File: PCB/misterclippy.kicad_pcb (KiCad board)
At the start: 2 copper layers, 75 parts, among them J1 PWR, J2 Output Gate, J3 Output Gate, J4 Input, J5 Input, J6 Through, J7 Through, J8 Audio In, J9 Audio In, Q1 BC547, Q2 BC547, U1 LM393, U2 TL072, U3 LM393, U4 TL072, U5 LM393

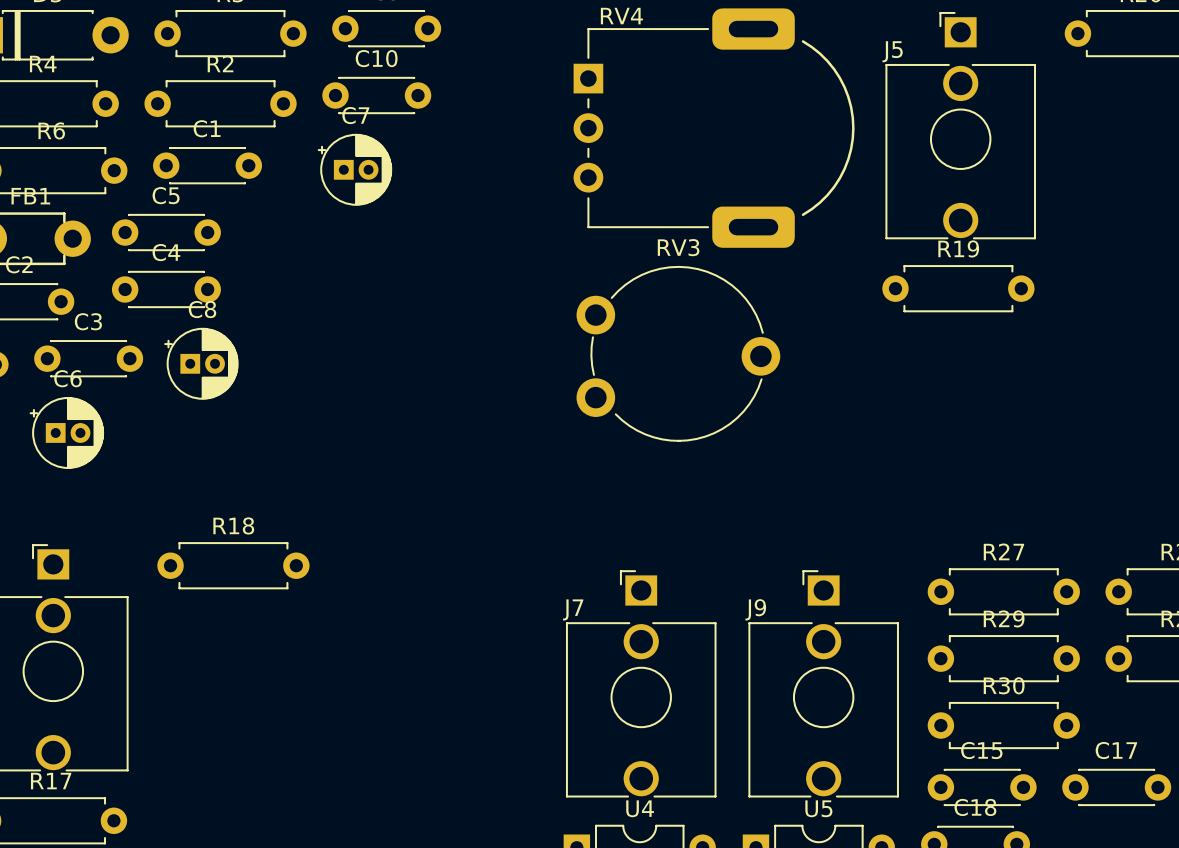
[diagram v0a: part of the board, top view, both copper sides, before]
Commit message: :wrench: Re-assign component designators
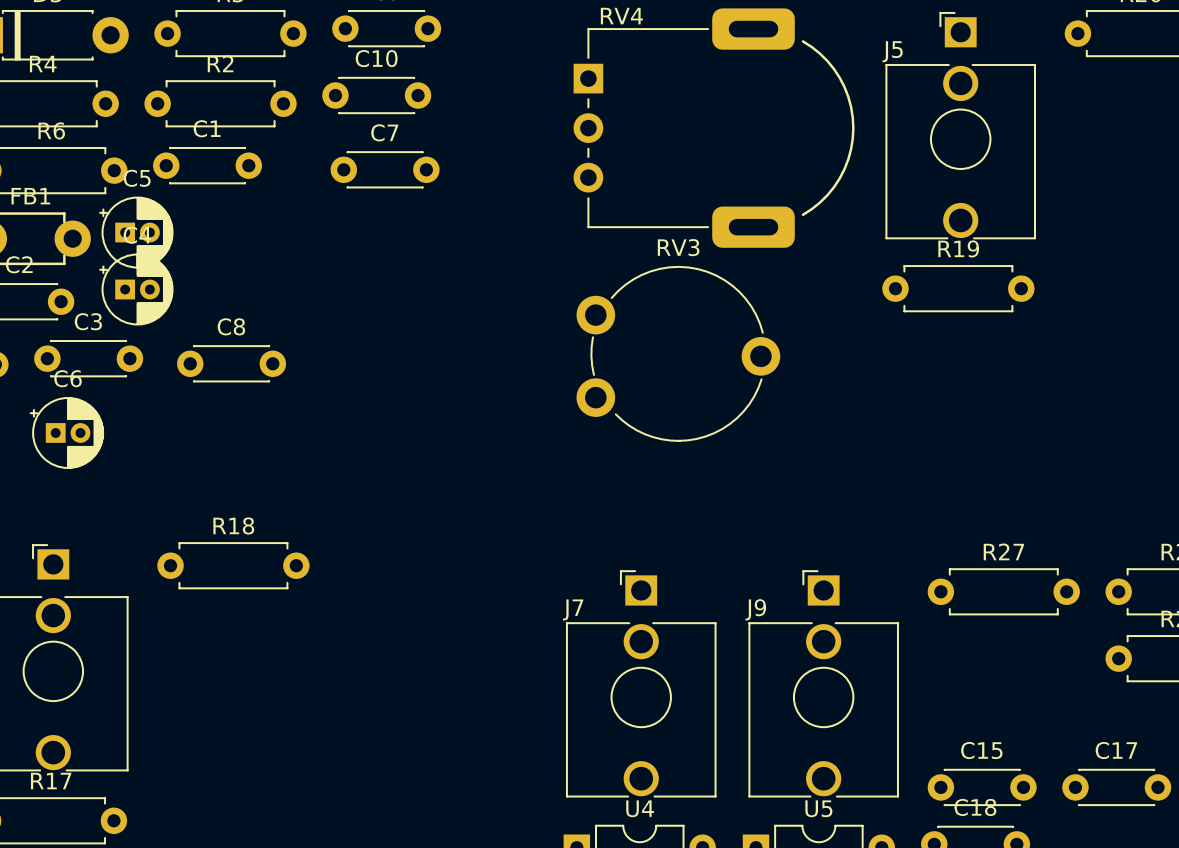
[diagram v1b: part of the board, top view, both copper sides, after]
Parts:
- removed R29, R30: 100k, Resistor_THT:R_Axial_DIN0207_L6.3mm_D2.5mm_P7.62mm_Horizontal
- C4, C5: value 100n -> 10u; footprint Capacitor_THT:C_Disc_D4.3mm_W1.9mm_P5.00mm -> Capacitor_THT:CP_Radial_D4.0mm_P1.50mm
- C7, C8: value 10u -> 100n; footprint Capacitor_THT:CP_Radial_D4.0mm_P1.50mm -> Capacitor_THT:C_Disc_D4.3mm_W1.9mm_P5.00mm
- J6: value Through -> Audio In
- J9: value Audio In -> Through
- R10, R15: value 2k2 -> 22k
- R11: value 10k -> 4k7
- R12, R7: value 22k -> 10k
- R13, R8: value 4k7 -> 2k2
- R16: value 10k -> 100k
- R19: value 22k -> 100k
- R22, R27: value 1k -> 100k
- R23, R28: value 100k -> 1k
- R5: value 47k -> 22k
- R6: value 100k -> 4k7
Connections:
- C1 pad 1: +12V -> +5V
- C10 pad 1: /Detector1/Clipped -> GND
- C2 pad 1: GND -> Net-(D2-K)
- C2 pad 2: -12V -> GND
- C3 pad 1: +5V -> GND
- C3 pad 2: GND -> Net-(D3-A)
- C4 pad 1: Net-(C4-Pad1) -> +5V
- C5 pad 1: GND -> +12V
- C5 pad 2: Net-(C5-Pad2) -> GND
- C6 pad 1: +5V -> GND
- C6 pad 2: GND -> -12V
- C7 pad 1: +12V -> /Detector 1/Clipped
- C7 pad 2: GND -> -12V
- C8 pad 1: GND -> /Detector 2/Clipped
- C9 pad 1: /Detector/Clipped -> +12V
- C9 pad 2: -12V -> GND
- D2 pad 1: Net-(C4-Pad1) -> Net-(D2-K)
- D3 pad 2: Net-(C5-Pad2) -> Net-(D3-A)
- D4 pad 1: Net-(D4-Pad1) -> Net-(D4-K)
- D5 pad 1: Net-(D5-Pad1) -> Net-(D5-K)
- FB1 pad 1: Net-(C4-Pad1) -> Net-(D2-K)
- FB2 pad 1: Net-(C5-Pad2) -> Net-(D3-A)
- J6 pad TN: unconnected-(J6-PadTN) -> GND
- J8 pad T: Net-(R21-Pad1) -> Net-(J8-PadT)
- J9 pad T: Net-(R26-Pad1) -> Net-(J9-PadT)
- J9 pad TN: GND -> unconnected-(J9-PadTN)
- Q1 pad 1: Net-(Q1-Pad1) -> Net-(Q1-C)
- Q1 pad 2: Net-(Q1-Pad2) -> Net-(Q1-B)
- Q2 pad 1: Net-(Q2-Pad1) -> Net-(Q2-C)
- Q2 pad 2: Net-(Q2-Pad2) -> Net-(Q2-B)
- R1 pad 2: /Detector/Clipped -> /Detector 1/Clipped
- R10 pad 1: +5V -> /Output 2/Clip Input
- R10 pad 2: Net-(Q1-Pad1) -> Net-(D5-K)
- R11 pad 1: Net-(Q1-Pad1) -> +5V
- R11 pad 2: Net-(J2-PadT) -> Net-(Q2-B)
- R12 pad 1: /output1/Clip Input -> Net-(Q2-B)
- R12 pad 2: Net-(D5-Pad1) -> /Output 2/Clip Input
- R13 pad 2: Net-(Q2-Pad2) -> Net-(Q2-C)
- R14 pad 1: Net-(Q2-Pad2) -> Net-(Q2-C)
- R14 pad 2: /output1/Clip Input -> Net-(J3-PadT)
- R15 pad 1: +5V -> +12V
- R15 pad 2: Net-(Q2-Pad1) -> Net-(R15-Pad2)
- R16 pad 1: Net-(Q2-Pad1) -> GND
- R16 pad 2: Net-(J3-PadT) -> Net-(R16-Pad2)
- R19 pad 1: +12V -> Net-(J6-PadT)
- R19 pad 2: Net-(R19-Pad2) -> Net-(U2A-+)
- R2 pad 2: /Detector1/Clipped -> /Detector 2/Clipped
- R20 pad 1: GND -> Net-(U3A--)
- R20 pad 2: Net-(R20-Pad2) -> /Clip CV 1/Clip CV
- R21 pad 1: Net-(R21-Pad1) -> Net-(U2B--)
- R21 pad 2: Net-(R21-Pad2) -> /Clip CV 1/Clip CV
- R22 pad 1: Audio Input -> Net-(U3B-+)
- R22 pad 2: Net-(J6-PadT) -> Net-(U2B--)
- R23 pad 1: Net-(R23-Pad1) -> Net-(J7-PadT)
- R23 pad 2: /Clip CV/Clip CV -> Net-(U2A--)
- R24 pad 1: Net-(R24-Pad1) -> Net-(J8-PadT)
- R24 pad 2: /Clip CV/Clip CV -> Net-(U4A-+)
- R25 pad 1: Net-(R25-Pad1) -> Net-(U5A--)
- R25 pad 2: Net-(R23-Pad1) -> /Clip CV 2/Clip CV
- R26 pad 1: Net-(R26-Pad1) -> Net-(U4B--)
- R26 pad 2: Net-(R26-Pad2) -> /Clip CV 2/Clip CV
- R27 pad 1: Audio Input -> Net-(U5B-+)
- R27 pad 2: Net-(J7-PadT) -> Net-(U4B--)
- R28 pad 1: Net-(R28-Pad1) -> Net-(J9-PadT)
- R28 pad 2: /Clip CV1/Clip CV -> Net-(U4A--)
- R3 pad 2: Net-(R3-Pad2) -> DELAY_THRESHOLD
- R4 pad 1: Net-(R3-Pad2) -> DELAY_THRESHOLD
- R5 pad 1: GND -> /Output 1/Clip Input
- R5 pad 2: Net-(R5-Pad2) -> Net-(D4-K)
- R6 pad 1: Net-(R5-Pad2) -> +5V
- R6 pad 2: -12V -> Net-(Q1-B)
- R7 pad 1: /output/Clip Input -> Net-(Q1-B)
- R7 pad 2: Net-(D4-Pad1) -> /Output 1/Clip Input
- R8 pad 2: Net-(Q1-Pad2) -> Net-(Q1-C)
- R9 pad 1: Net-(Q1-Pad2) -> Net-(Q1-C)
- R9 pad 2: /output/Clip Input -> Net-(J2-PadT)
- RV1 pad 1: Net-(R17-Pad2) -> Net-(R15-Pad2)
- RV1 pad 3: Net-(R18-Pad2) -> Net-(R16-Pad2)
- RV2 pad 2: /Clip CV/Clip CV -> /Clip CV 1/Clip CV
- RV3 pad 1: Net-(R19-Pad2) -> Net-(R17-Pad2)
- RV3 pad 3: Net-(R20-Pad2) -> Net-(R18-Pad2)
- RV4 pad 2: /Clip CV1/Clip CV -> /Clip CV 2/Clip CV
- U1 pad 1: /output/Clip Input -> /Output 1/Clip Input
- U1 pad 2: /Detector/Clipped -> /Detector 1/Clipped
- U1 pad 3: Net-(R3-Pad2) -> DELAY_THRESHOLD
- U1 pad 5: Net-(R5-Pad2) -> DELAY_THRESHOLD
- U1 pad 6: /Detector1/Clipped -> /Detector 2/Clipped
- U1 pad 7: /output1/Clip Input -> /Output 2/Clip Input
- U2 pad 1: Audio Input -> Net-(U2A--)
- U2 pad 2: Audio Input -> Net-(U2A--)
- U2 pad 3: Net-(R21-Pad2) -> Net-(U2A-+)
- U2 pad 6: Net-(R23-Pad1) -> Net-(U2B--)
- U2 pad 7: Net-(R25-Pad1) -> Net-(U3B-+)
- U3 pad 1: /Detector/Clipped -> /Detector 1/Clipped
- U3 pad 2: Net-(R24-Pad1) -> Net-(U3A--)
- U3 pad 3: Audio Input -> Net-(U2A--)
- U3 pad 5: Net-(R25-Pad1) -> Net-(U3B-+)
- U3 pad 6: Audio Input -> Net-(U2A--)
- U3 pad 7: /Detector/Clipped -> /Detector 1/Clipped
- U4 pad 1: Audio Input -> Net-(U4A--)
- U4 pad 2: Audio Input -> Net-(U4A--)
- U4 pad 3: Net-(R26-Pad2) -> Net-(U4A-+)
- U4 pad 6: Net-(R28-Pad1) -> Net-(U4B--)
- U4 pad 7: Net-(R30-Pad1) -> Net-(U5B-+)
- U5 pad 1: /Detector1/Clipped -> /Detector 2/Clipped
- U5 pad 2: Net-(R29-Pad1) -> Net-(U5A--)
- U5 pad 3: Audio Input -> Net-(U4A--)
- U5 pad 5: Net-(R30-Pad1) -> Net-(U5B-+)
- U5 pad 6: Audio Input -> Net-(U4A--)
- U5 pad 7: /Detector1/Clipped -> /Detector 2/Clipped

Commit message: PCB layout ready for production
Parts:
- C1, C10, C11, C12, C13, C14, C15, C16, C17, C18, C2, C3, C4, C5, C6, C7, C8, C9, D1, D2, D3, FB1, FB2, J1, Q1, Q2, R1, R10, R11, R12, R13, R14, R15, R16, R17, R18, R19, R2, R20, R22, R23, R24, R25, R27, R28, R3, R4, R5, R6, R7, R8, R9, RV1, RV3, U1, U2, U3, U4, U5: moved to B.Cu
- J2, J3, J4, J5, J6, J7, J8, J9: footprint Connector_Audio:Jack_3.5mm_QingPu_WQP-PJ398SM_Vertical_CircularHoles -> mopsy:Jack_3.5mm_QingPu_WQP-PJ398SM_Vertical_CircularHoles_Centered
- R21, R26: footprint Resistor_THT:R_Axial_DIN0207_L6.3mm_D2.5mm_P7.62mm_Horizontal -> Resistor_THT:R_Axial_DIN0207_L6.3mm_D2.5mm_P2.54mm_Vertical; moved to B.Cu
- moved U1 107.0 mm to (116.1, 155.6)
- moved R4 104.6 mm to (124.0, 158.6)
- moved C9 100.8 mm to (121.9, 158.6), turned to 180 degrees
- moved R2 100.4 mm to (130.3, 156.1), turned to 90 degrees
- moved R3 99.7 mm to (107.2, 158.6)
- moved C13 93.3 mm to (105.7, 74.2), turned to -90 degrees
- moved R21 92.7 mm to (109.1, 67.9), turned to -90 degrees
- moved C10 91.5 mm to (114.0, 154.6), turned to 90 degrees
- moved R23 91.3 mm to (113.5, 88.9), turned to 180 degrees
- moved R22 85.1 mm to (105.9, 54.4), turned to -90 degrees
- moved R6 83.9 mm to (123.4, 139.4), turned to 180 degrees
- moved R1 83.5 mm to (109.1, 148.6), turned to -90 degrees
- moved C7 79.5 mm to (122.4, 145.0), turned to 180 degrees
- moved J1 79.5 mm to (111.3, 121.9), turned to -90 degrees
- moved D1 77.4 mm to (118.6, 130.2)
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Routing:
- net +12V: track 0.00 -> 237.1 mm, vias 0 -> 2
- net -12V: track 0.00 -> 170.3 mm, vias 0 -> 2
- net /Detector 1/Clipped: track 0.00 -> 113.5 mm, vias 0 -> 2
- net /Detector 2/Clipped: track 0.00 -> 96.6 mm
- net +5V: track 0.00 -> 73.2 mm
- net Net-(U4A--): track 0.00 -> 55.3 mm, vias 0 -> 2
- net Net-(U2A--): track 0.00 -> 44.0 mm
- net GND: track 0.00 -> 39.8 mm, vias 0 -> 38
- net Net-(J5-PadT): track 0.00 -> 38.0 mm
- net Net-(J9-PadT): track 0.00 -> 37.1 mm, vias 0 -> 2
- net Net-(J4-PadT): track 0.00 -> 35.1 mm
- net Net-(U5B-+): track 0.00 -> 33.5 mm
- net /Clip CV 1/Clip CV: track 0.00 -> 31.3 mm
- net DELAY_THRESHOLD: track 0.00 -> 30.2 mm
- net Net-(U3B-+): track 0.00 -> 30.2 mm
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- added copper zone on B.Cu, net GND
- added copper zone on F.Cu, net GND
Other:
- board outline added: 30.2 x 109.2 mm
- board text added: "CC-BY-SA 4.0 Patrick Pickel Stefan Haun"
- board text added: "github.com/rainerhassel/MisterClippy"

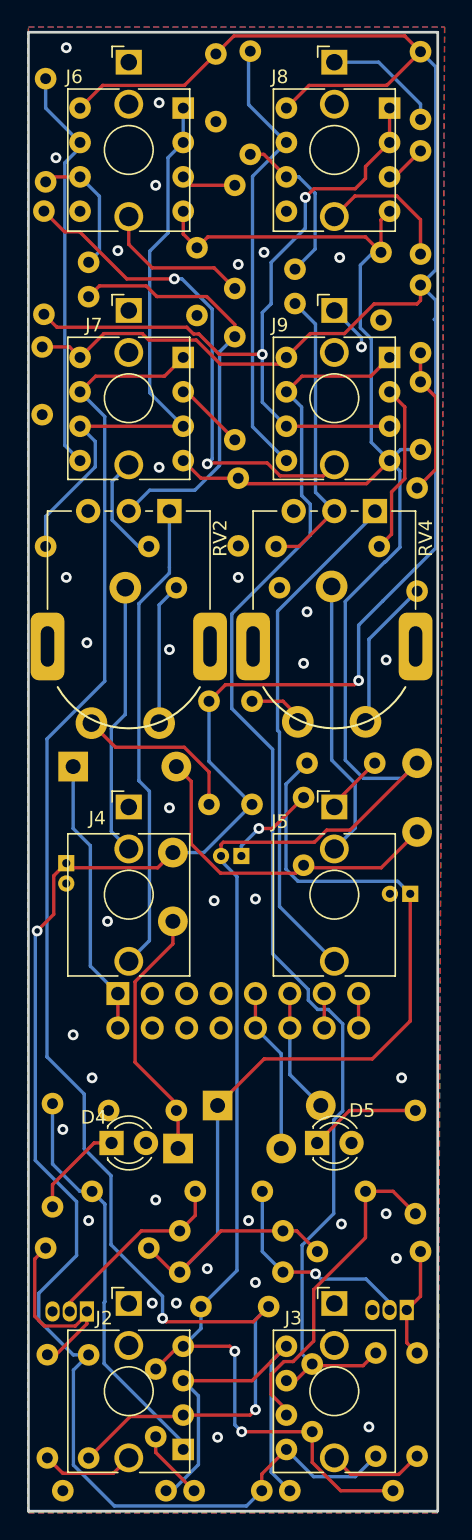
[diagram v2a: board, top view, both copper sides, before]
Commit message: :art: Try for a design where ICs do not cover jacks
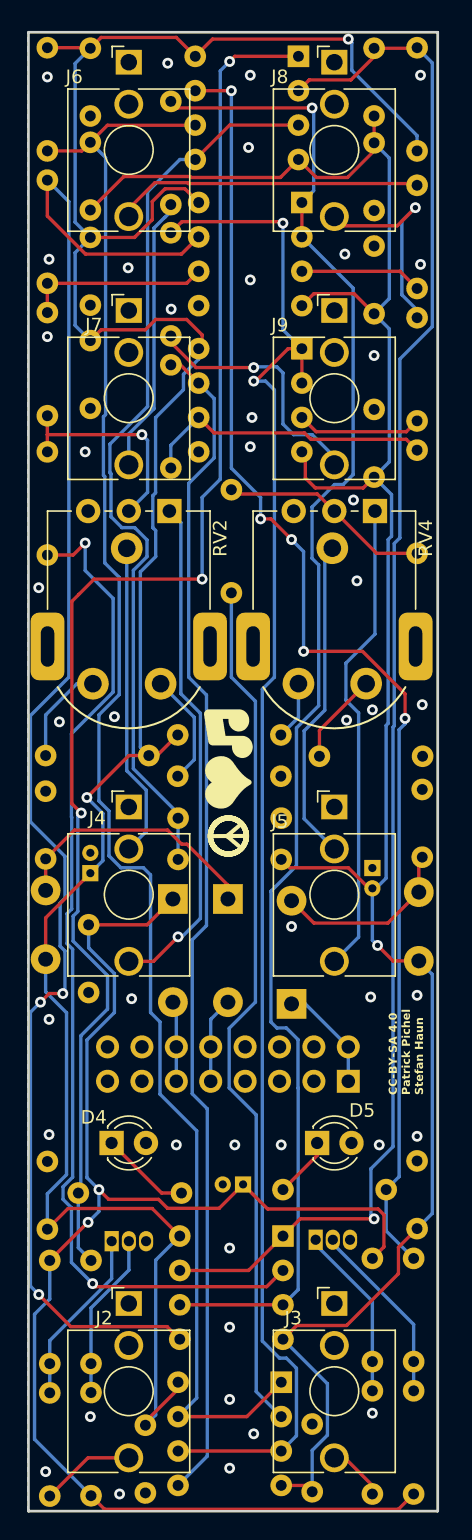
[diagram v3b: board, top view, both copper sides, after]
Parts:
- R21, R26: footprint Resistor_THT:R_Axial_DIN0207_L6.3mm_D2.5mm_P2.54mm_Vertical -> Resistor_THT:R_Axial_DIN0207_L6.3mm_D2.5mm_P7.62mm_Horizontal
- moved C9 107.3 mm to (109.2, 52.1), turned to -90 degrees
- moved R2 106.8 mm to (106.0, 52.1), turned to -90 degrees
- moved U1 103.2 mm to (124.6, 52.7), turned to 180 degrees
- moved C7 93.2 mm to (130.2, 52.1), turned to -90 degrees
- moved R1 92.2 mm to (133.3, 59.7), turned to 90 degrees
- moved C10 92.0 mm to (130.2, 64.1)
- moved C8 91.7 mm to (109.2, 59.1)
- moved C17 86.6 mm to (113.3, 153.8)
- moved C18 77.4 mm to (125.6, 153.7)
- moved U5 76.1 mm to (123.3, 150.6)
- moved U3 65.3 mm to (123.4, 139.8)
- moved C13 65.2 mm to (106.0, 139.3), turned to 90 degrees
- moved R3 52.2 mm to (123.3, 109.0), turned to 180 degrees
- moved R4 47.3 mm to (115.7, 112.0)
- moved C14 47.3 mm to (133.3, 134.3), turned to -90 degrees
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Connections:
- J1 pad 13: CV -> unconnected-(J1-Pin_13-Pad13)
- J1 pad 14: CV -> unconnected-(J1-Pin_14-Pad14)
- J1 pad 15: Gate -> unconnected-(J1-Pin_15-Pad15)
- J1 pad 16: Gate -> unconnected-(J1-Pin_16-Pad16)
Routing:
- net Net-(U3B-+): track 30.2 -> 114.6 mm, vias 0 -> 3
- net /Output 1/Clip Input: track 30.1 -> 106.1 mm, vias 0 -> 3
- net /Output 2/Clip Input: track 24.9 -> 98.6 mm, vias 0 -> 5
- net Net-(U3A--): track 5.28 -> 76.2 mm, vias 0 -> 2
- net Net-(U2A--): track 44.0 -> 113.6 mm, vias 0 -> 1
- net Net-(U4A--): track 55.3 -> 115.6 mm
- net Net-(U5B-+): track 33.5 -> 87.6 mm
- net +12V: track 237.1 -> 185.3 mm
- net Net-(U5A--): track 12.7 -> 64.0 mm
- net GND: track 39.8 -> 0.00 mm, vias 38 -> 44
- net DELAY_THRESHOLD: track 30.2 -> 67.1 mm
- net +5V: track 73.2 -> 106.4 mm, vias 0 -> 2
- net /Detector 2/Clipped: track 96.6 -> 120.7 mm
- net Net-(J9-PadT): track 37.1 -> 18.9 mm, vias 2 -> 1
- net /Clip CV 1/Clip CV: track 31.3 -> 16.0 mm, vias 0 -> 1
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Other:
- board text added: "CC-BY-SA 4.0 Patrick Pichel Stefan Haun"
- board text added: "Red Stripe -12V"
- board text added: "v1"
- board text removed: "CC-BY-SA 4.0 Patrick Pickel Stefan Haun"

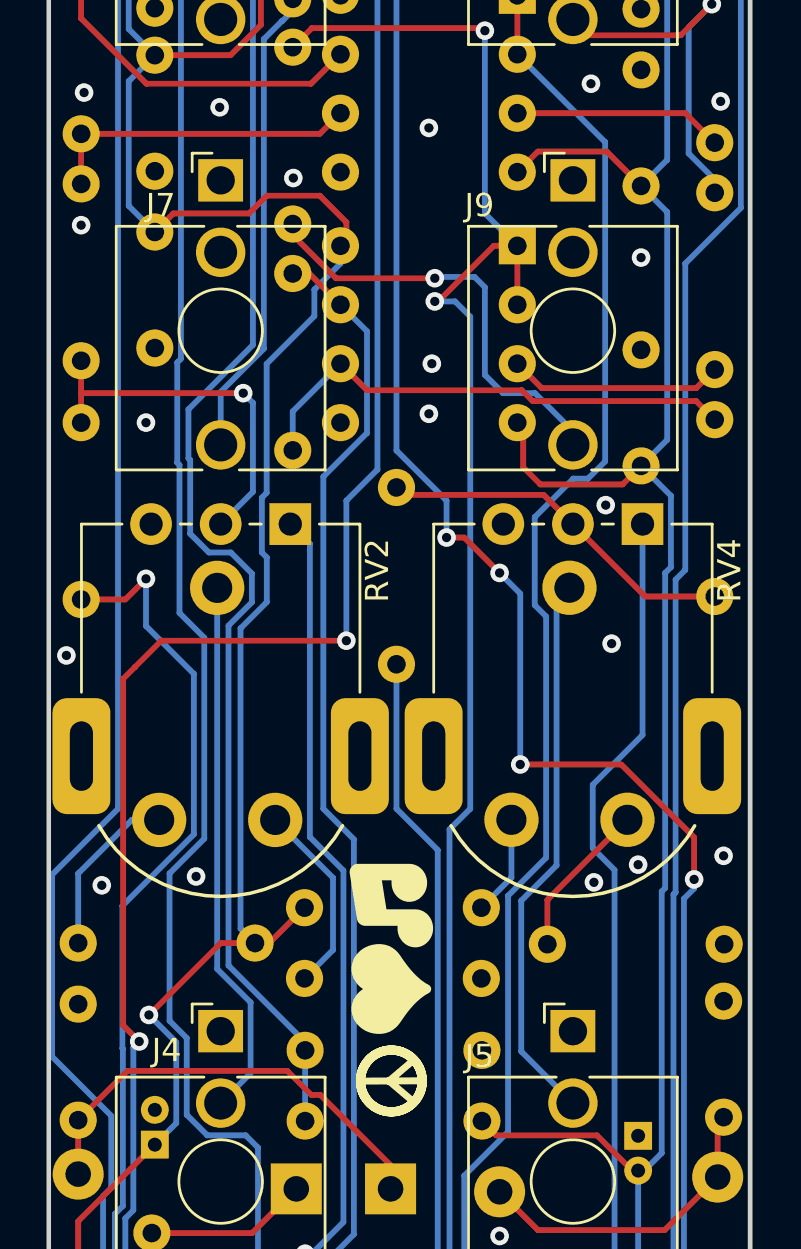
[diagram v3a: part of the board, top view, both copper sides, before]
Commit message: :hammer: Adapt PCB to fixed poti directions
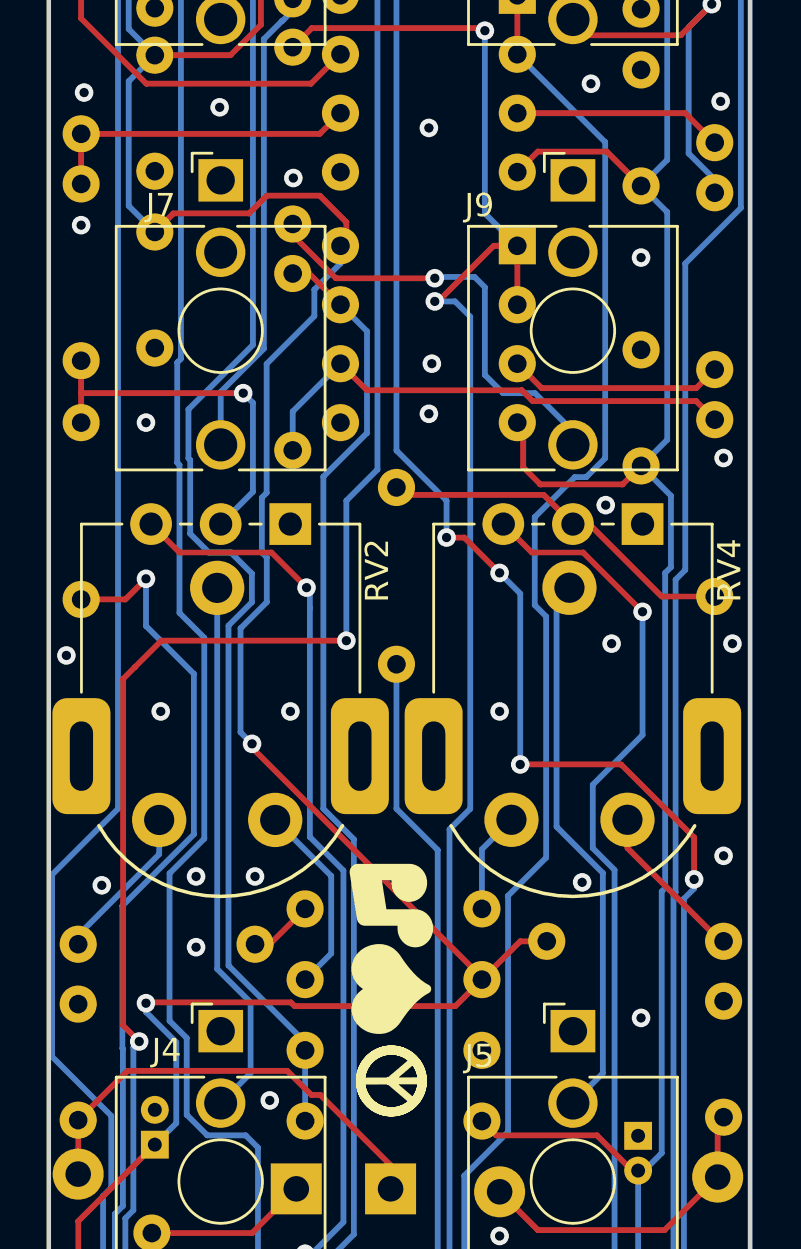
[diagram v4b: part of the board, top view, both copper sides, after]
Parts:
- moved R18 18.1 mm to (115.7, 102.9), turned to 0 degrees
- moved R17 10.5 mm to (126.1, 104.3)
- moved R15 9.90 mm to (123.3, 105.9)
- moved R16 9.86 mm to (113.5, 104.4)
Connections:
- RV1 pad 1: Net-(R15-Pad2) -> Net-(R16-Pad2)
- RV1 pad 3: Net-(R16-Pad2) -> Net-(R15-Pad2)
- RV2 pad 1: Net-(J4-PadT) -> GND
- RV2 pad 3: GND -> Net-(J4-PadT)
- RV3 pad 1: Net-(R17-Pad2) -> Net-(R18-Pad2)
- RV3 pad 3: Net-(R18-Pad2) -> Net-(R17-Pad2)
- RV4 pad 1: Net-(J5-PadT) -> GND
- RV4 pad 3: GND -> Net-(J5-PadT)
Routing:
- net +12V: track 185.3 -> 201.3 mm, vias 2 -> 3
- net Net-(J4-PadT): track 37.6 -> 42.4 mm, vias 1 -> 2
- net Net-(J5-PadT): track 35.3 -> 39.1 mm, vias 0 -> 1
- net GND: track 0.00 -> 3.40 mm, vias 44 -> 52
- net Net-(R17-Pad2): track 4.33 -> 7.03 mm
- net Net-(R18-Pad2): track 6.79 -> 4.37 mm
- net Net-(R16-Pad2): track 8.37 -> 6.80 mm
- net Net-(R15-Pad2): track 7.44 -> 8.35 mm

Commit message: :pencil2: Replace Befaco 12mm poti footprint with fixed verion
Use footprint based on https://github.com/moPsy-project/moPsy-KiCad-resources/pull/14
and adjust traces accordingly
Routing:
- net -12V: track 164.7 -> 165.5 mm
- net Net-(J5-PadT): track 39.1 -> 39.6 mm
- net Net-(J4-PadT): track 42.4 -> 42.9 mm
